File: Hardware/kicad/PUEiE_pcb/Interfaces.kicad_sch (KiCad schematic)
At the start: 45 parts, among them J301 JST_PHx04, J302 JST_PHx04, J303 Conn_IPEX, J304 Conn_01x03, Q301A301 PMOS, Q301B301 NMOS, U301 MAX-M10S-00B, U302 LIS3MDL, U303 TMC2208-LA, U305 NC7WZ07P6X

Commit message: Board Setup
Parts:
- removed Q301A301: PMOS, Package_SO:SOP-8_3.76x4.96mm_P1.27mm, symbol Simulation_SPICE:PMOS
- removed Q301B301: NMOS, Package_SO:SOP-8_3.76x4.96mm_P1.27mm, symbol Simulation_SPICE:NMOS
- added Q301: ZXMC4559DN8TA, Package_SO:SOP-8_3.76x4.96mm_P1.27mm, symbol PUEiE_pcb_schematic_symbols:ZXMC4559DN8TA
- renumbered C319 to C301, C303 to C302, C301 to C303, C302 to C304, C304 to C305, C313 to C306, C306 to C307, C307 to C308, C308 to C309, C309 to C310, C310 to C311, C311 to C312, C312 to C313, J303 to J301, J301 to J302, J302 to J303, JP306 to JP304, JP304 to JP305, JP305 to JP306, R308 to R302, R302 to R303, R303 to R304, R307 to R305, R309 to R306, R304 to R307, R305 to R308, R306 to R309, U305 to U302, U302 to U303, U303 to U304
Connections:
- net GND: now also Q301.1 (S1)
- net LNA_EN: now also Q301.2 (G1)
- net PMOS_D: now also Q301.5 (D2), Q301.6 (D1)
- net PMOS_G: now also Q301.4 (G2), Q301.7 (D1), Q301.8 (D1)
- net VCC_RF: now also Q301.3 (S2)
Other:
- moved on the sheet: C302, R301

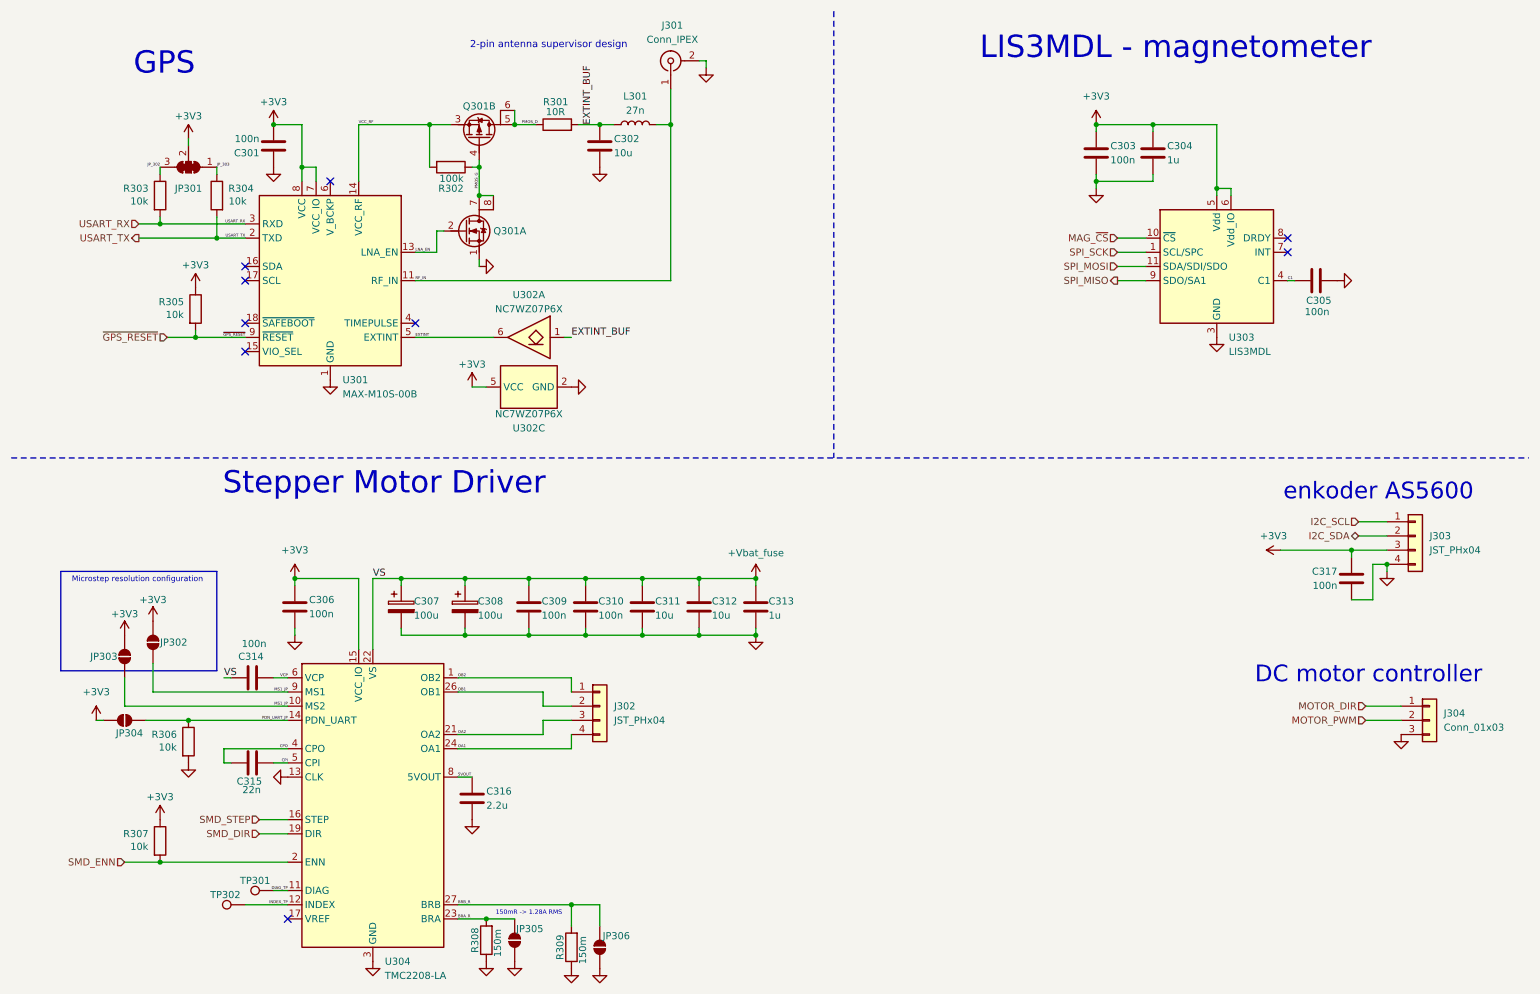
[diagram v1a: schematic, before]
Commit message: pcb placement
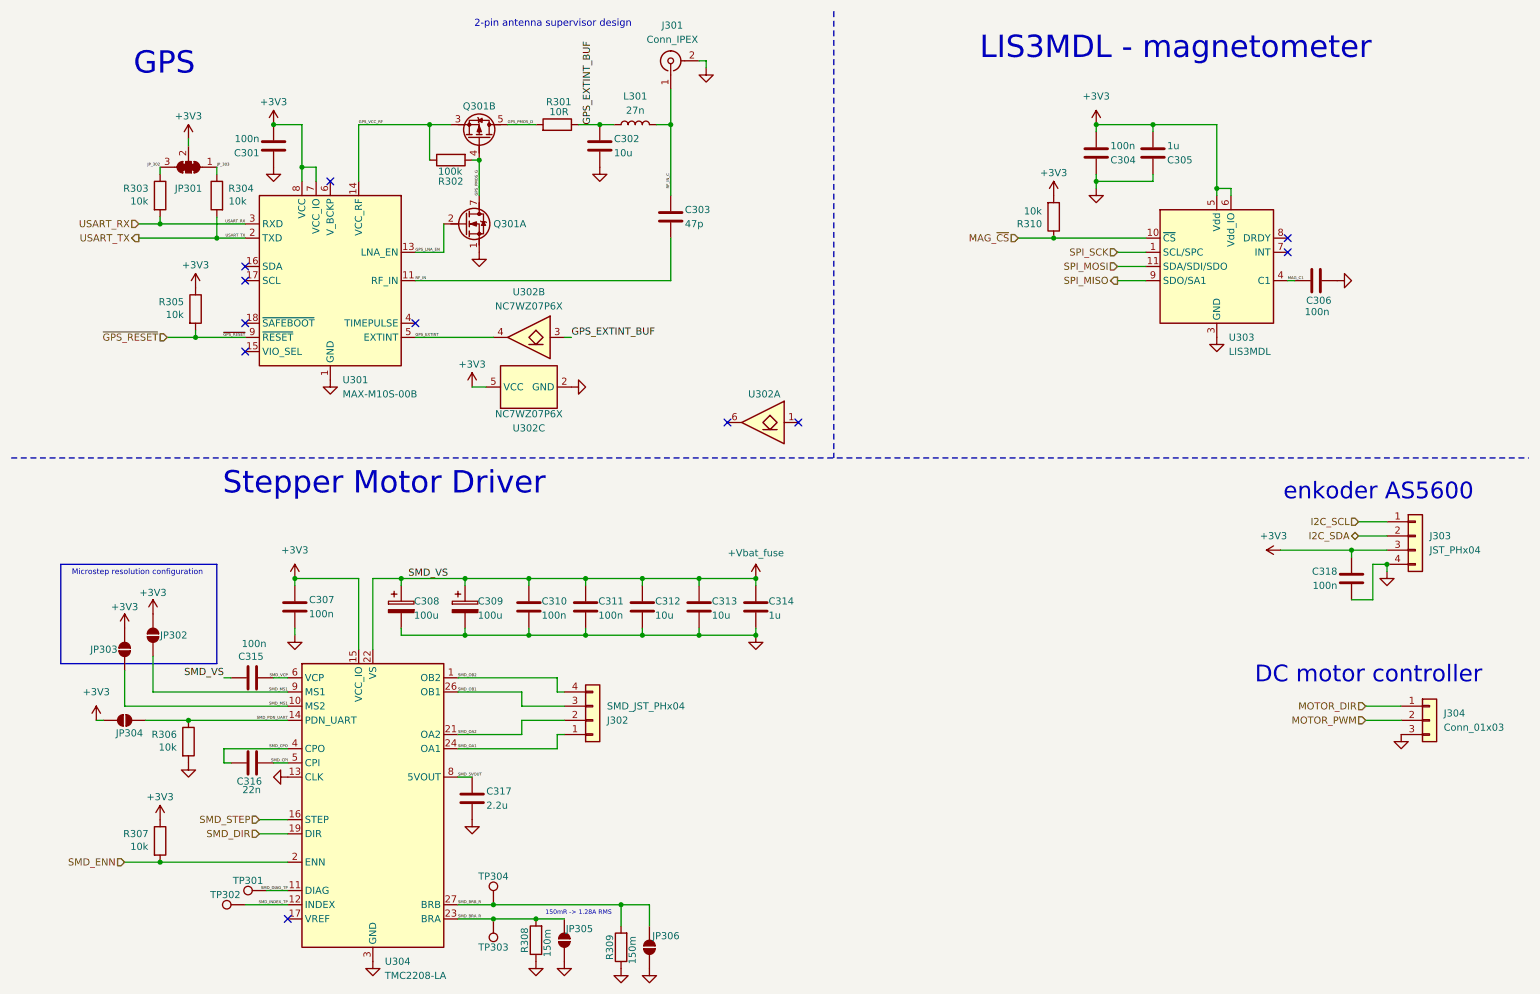
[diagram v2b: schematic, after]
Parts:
- added C303: 47p, Capacitor_SMD:C_0805_2012Metric, symbol Device:C
- added R310: 10k, Resistor_SMD:R_0805_2012Metric, symbol Device:R
- added TP303, TP304: TestPoint, TestPoint:TestPoint_Pad_D2.0mm, symbol Connector:TestPoint
- added unit 2 of U302
- J302: value JST_PHx04 -> SMD_JST_PHx04
- JP301: footprint Jumper:SolderJumper-2_P1.3mm_Open_TrianglePad1.0x1.5mm -> Jumper:SolderJumper-3_P2.0mm_Open_TrianglePad1.0x1.5mm
- U301: MFR Part MAX-M10S-00B -> MAX-M10S-00B
- U302: MFR Part NC7WZ07P6X -> NC7WZ07P6X
- U303: MFR Part LIS3MDLTR -> LIS3MDLTR
- U304: footprint Package_DFN_QFN:TQFN-32-1EP_5x5mm_P0.5mm_EP3.4x3.4mm_ThermalVias -> Package_DFN_QFN:QFN-28-1EP_5x5mm_P0.5mm_EP3.75x3.75mm_ThermalVias
- renumbered C303 to C304, C304 to C305, C305 to C306, C306 to C307, C307 to C308, C308 to C309, C309 to C310, C310 to C311, C311 to C312, C312 to C313, C313 to C314, C314 to C315, C315 to C316, C316 to C317, C317 to C318
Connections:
- net +3V3: now also C304.2, C305.2, R310.2; no longer C304.1, C305.1
- net GND: now also C304.1, C305.1, U304.29 (GND); no longer C304.2, C305.2
- net MAG_~{CS}: now also R310.1
- net RF_IN: now also C303.2; no longer J301.1 (In), L301.2
- net 5VOUT renamed SMD_5VOUT
- net BRA_R renamed SMD_BRA_R
- net SMD_BRA_R: now also TP303.1
- net BRB_R renamed SMD_BRB_R
- net SMD_BRB_R: now also TP304.1
- net C1 renamed MAG_C1
- net CPI renamed SMD_CPI
- net CPO renamed SMD_CPO
- net DIAG_TP renamed SMD_DIAG_TP
- net EXTINT: no longer names the net of U302.6
- net EXTINT: no longer U301.5 (EXTINT)
- net EXTINT_BUF renamed GPS_EXTINT_BUF
- net GPS_EXTINT_BUF: now also R301.1, U302.3; no longer R301.2, U302.1
- net INDEX_TP renamed SMD_INDEX_TP
- net LNA_EN renamed GPS_LNA_EN
- net MS1_JP renamed SMD_MS1
- net OA1 renamed SMD_OA1
- net SMD_OA1: now also J302.1 (Pin_1); no longer J302.4 (Pin_4)
- net OA2 renamed SMD_OA2
- net SMD_OA2: now also J302.2 (Pin_2); no longer J302.3 (Pin_3)
- net OB1 renamed SMD_OB1
- net SMD_OB1: now also J302.3 (Pin_3); no longer J302.2 (Pin_2)
- net OB2 renamed SMD_OB2
- net SMD_OB2: now also J302.4 (Pin_4); no longer J302.1 (Pin_1)
- net PDN_UART_JP renamed SMD_PDN_UART
- net PMOS_D renamed GPS_PMOS_D
- net GPS_PMOS_D: now also R301.2; no longer R301.1
- net PMOS_G renamed GPS_PMOS_G
- net GPS_PMOS_G: now also R302.2; no longer R302.1
- net VCC_RF renamed GPS_VCC_RF
- net GPS_VCC_RF: now also R302.1; no longer R302.2
- net VCP renamed SMD_VCP
- new net GPS_EXTINT: U301.5 (EXTINT), U302.4
- new net RF_IN_C: C303.1, J301.1 (In), L301.2
- no-connect marks 9 -> 11
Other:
- moved on the sheet: J302, JP302, JP303, JP305, JP306, R301, R302, R308, R309, TP301

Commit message: PCB layout
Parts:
- removed C311: 100n, Capacitor_SMD:C_0805_2012Metric, symbol Device:C
- removed C313: 10u, Capacitor_SMD:C_0805_2012Metric, symbol Device:C
- removed C314: 1u, Capacitor_SMD:C_0805_2012Metric, symbol Device:C
- removed J304: Conn_01x03, Connector_JST:JST_XH_S3B-XH-A_1x03_P2.50mm_Horizontal, symbol Connector_Generic:Conn_01x03
- removed JP305, JP306: SolderJumper_2_Open, Jumper:SolderJumper-2_P1.3mm_Open_TrianglePad1.0x1.5mm, symbol Jumper:SolderJumper_2_Open
- removed TP303, TP304: TestPoint, TestPoint:TestPoint_Pad_D2.0mm, symbol Connector:TestPoint
- added C312: 10u, Capacitor_SMD:C_1206_3216Metric, symbol Device:C
- added FL301: SAW_GNSS, Filter:Filter_1109-5_1.1x0.9mm, symbol Filter:SAFFB1G58KA0F0A
- added J304: JST_PHx04, Connector_JST:JST_XH_S4B-XH-A_1x04_P2.50mm_Horizontal, symbol Connector_Generic:Conn_01x04
- C311: renamed from C312; footprint Capacitor_SMD:C_0805_2012Metric -> Capacitor_SMD:C_1206_3216Metric; Distributor https://jlcpcb.com/partdetail/367931-GRM21BR61E106MA73L/C39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 -> https://jlcpcb.com/partdetail/14236-CL31A106KBHNNNE/C13585; MFR Part GRM21BR61E106MA73L -> CL31A106KBHNNNE; Manufacturer Murata Electronics -> Samsung Electro-Mechanics
- renumbered C315 to C313, C316 to C314, C317 to C315, C318 to C316
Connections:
- net +3V3: now also J304.3 (Pin_3)
- net +Vbat_fuse: now also C312.1
- net GND: now also C312.2, FL301.2, FL301.3, FL301.5, J304.4 (Pin_4)
- net MOTOR_DIR: now also J304.1 (Pin_1)
- net MOTOR_PWM: now also J304.2 (Pin_2)
- net RF_IN: now also FL301.4; no longer C303.2
- net SMD_MS1: no longer JP303.2 (B), U304.10 (MS2)
- net SMD_OA1: now also U304.21 (OA2); no longer U304.24 (OA1)
- net SMD_OA2: now also U304.24 (OA1); no longer U304.21 (OA2)
- new net RF_IN_SAW: C303.2, FL301.1
- new net SMD_MS2: JP303.2 (B), U304.10 (MS2)
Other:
- moved on the sheet: C303, C311, J301, U302B

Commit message: Final PCB design
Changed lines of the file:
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@@
+		)
+	)
+	(polyline
+		(pts
+			(xy 217.17 92.71) (xy 217.17 165.1)
+		)
+		(stroke
+			(width 0)
+			(type dash_dot)
+			(color 0 0 0 1)
 		)
 	)
